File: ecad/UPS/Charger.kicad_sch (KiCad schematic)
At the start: 23 parts, among them Q1 NMOS, Q2 NMOS, Q3 NMOS, Q4 NMOS, U1 BQ25731RSNR

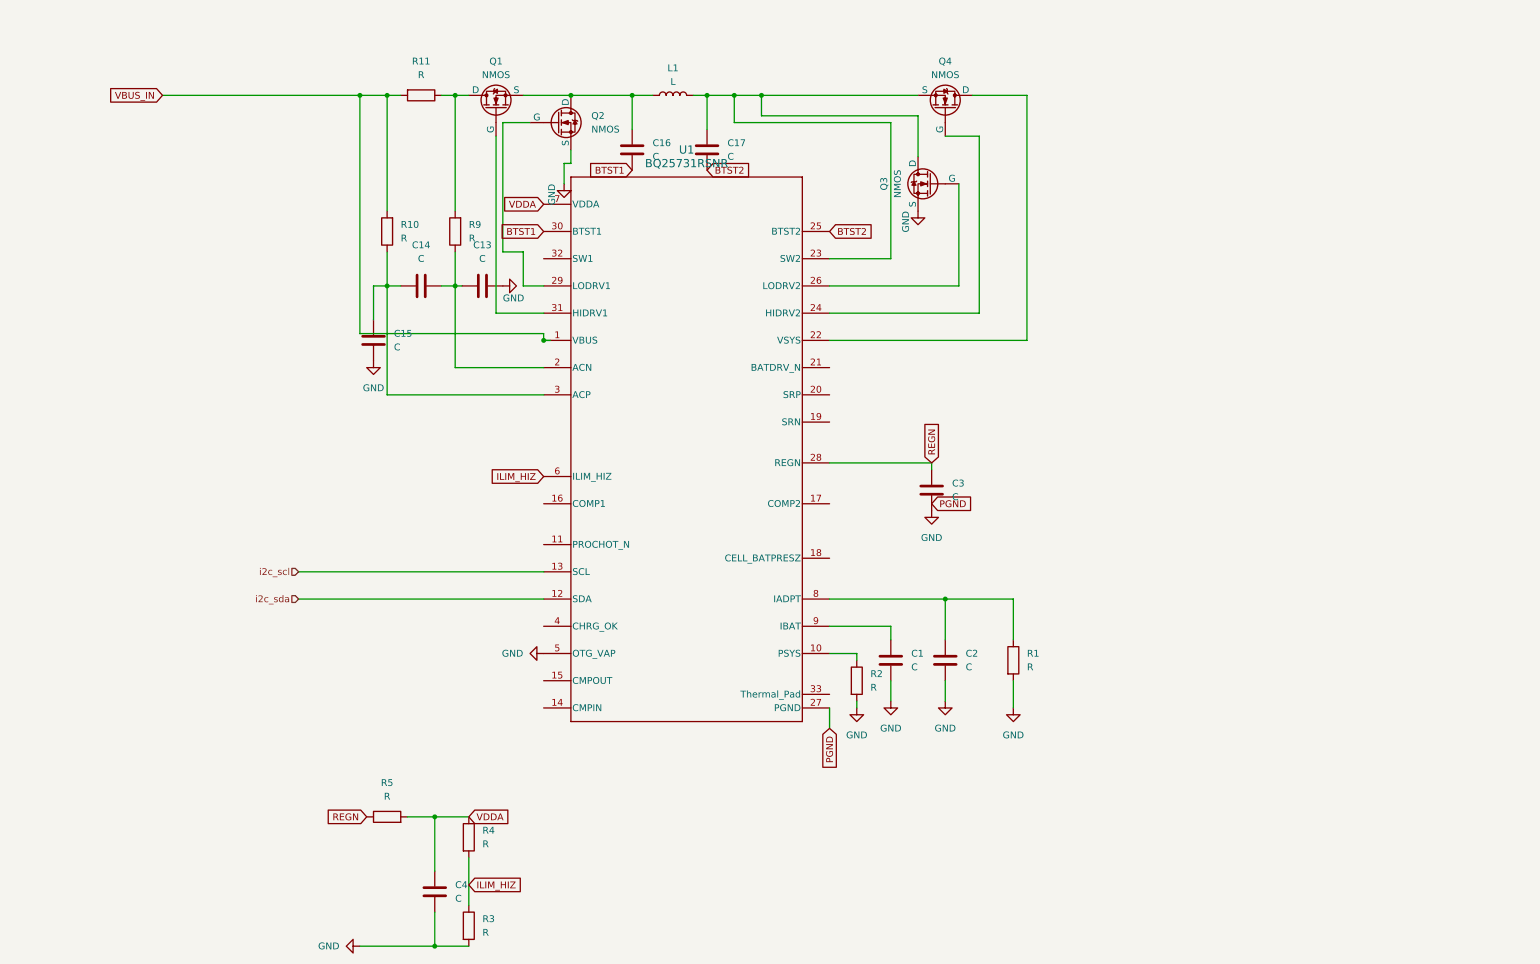
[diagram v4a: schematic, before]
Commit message: Complete most of the charger schematic
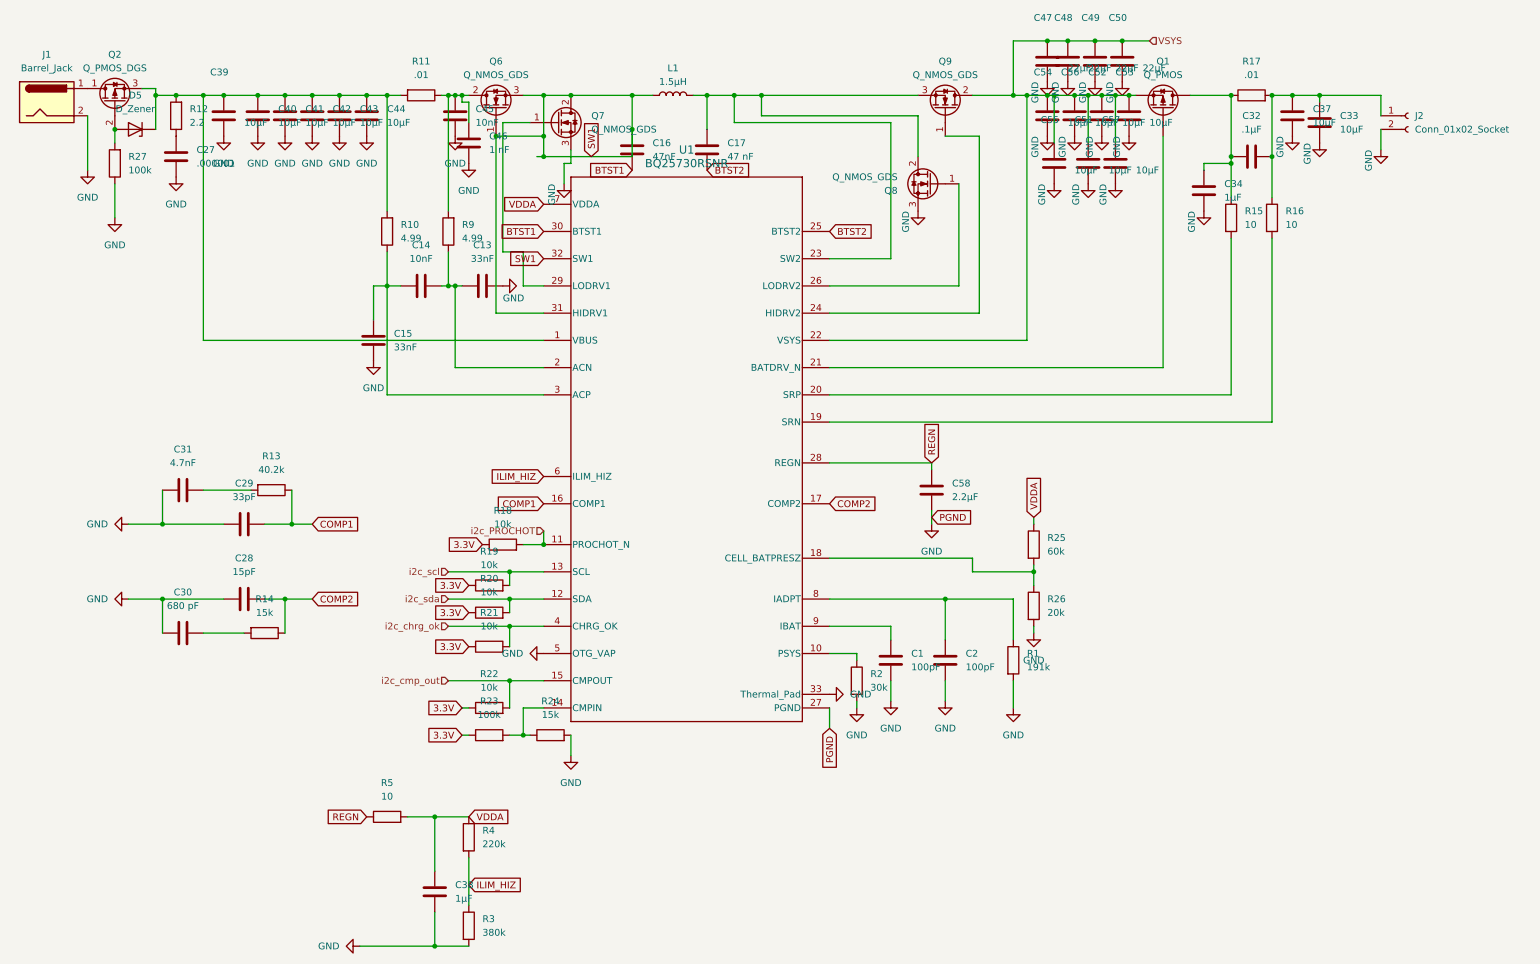
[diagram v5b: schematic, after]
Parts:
- removed C3, C4: C, symbol Device:C
- removed Q1, Q2, Q3, Q4: NMOS, symbol Simulation_SPICE:NMOS
- removed U1: BQ25731RSNR, UPS:RSN0032B-IPC_A, symbol UPS:BQ25731RSNR
- added C27: .000001, Capacitor_SMD:C_0603_1608Metric, symbol Device:C
- added C28: 15pF, Capacitor_SMD:C_0603_1608Metric, symbol Device:C
- added C29: 33pF, Capacitor_SMD:C_0603_1608Metric, symbol Device:C
- added C30: 680 pF, Capacitor_SMD:C_0603_1608Metric, symbol Device:C
- added C31: 4.7nF, Capacitor_SMD:C_0603_1608Metric, symbol Device:C
- added C32: .1µF, Capacitor_SMD:C_0603_1608Metric, symbol Device:C
- added C33, C37, C39, C40, C41, C42, C43, C44, C51, C52, C53, C54, C55, C56, C57: 10µF, Capacitor_SMD:C_0603_1608Metric, symbol Device:C
- added C34, C38: 1µF, Capacitor_SMD:C_0603_1608Metric, symbol Device:C
- added C45: 10nF, Capacitor_SMD:C_0603_1608Metric, symbol Device:C
- added C46: 1 nF, Capacitor_SMD:C_0603_1608Metric, symbol Device:C
- added C47, C48, C49, C50: 22µF, Capacitor_SMD:C_1206_3216Metric, symbol Device:C
- added C58: 2.2µF, Capacitor_SMD:C_0603_1608Metric, symbol Device:C
- added D5: D_Zener, symbol Device:D_Zener
- added J1: Barrel_Jack, symbol Connector:Barrel_Jack
- added J2: Conn_01x02_Socket, symbol Connector:Conn_01x02_Socket
- added Q1: Q_PMOS, symbol Device:Q_PMOS
- added Q2: Q_PMOS_DGS, symbol Transistor_FET:Q_PMOS_DGS
- added Q6, Q7, Q8, Q9: Q_NMOS_GDS, symbol Transistor_FET:Q_NMOS_GDS
- added R12: 2.2, Resistor_SMD:R_0805_2012Metric, symbol Device:R
- added R13: 40.2k, Resistor_SMD:R_0805_2012Metric, symbol Device:R
- added R14, R24: 15k, Resistor_SMD:R_0805_2012Metric, symbol Device:R
- added R15, R16: 10, Resistor_SMD:R_0805_2012Metric, symbol Device:R
- added R17: .01, Resistor_SMD:R_2512_6332Metric, symbol Device:R
- added R18, R19, R20, R21, R22: 10k, Resistor_SMD:R_0805_2012Metric, symbol Device:R
- added R23, R27: 100k, Resistor_SMD:R_0805_2012Metric, symbol Device:R
- added R25: 60k, Resistor_SMD:R_0805_2012Metric, symbol Device:R
- added R26: 20k, Resistor_SMD:R_0805_2012Metric, symbol Device:R
- added U1: BQ25730RSNR, UPS:RSN0032B-IPC_A, symbol UPS:BQ25730RSNR
- C1, C2: value C -> 100pF; footprint (none) -> Capacitor_SMD:C_0603_1608Metric
- C13, C15: value C -> 33nF; footprint (none) -> Capacitor_SMD:C_0603_1608Metric
- C14: value C -> 10nF; footprint (none) -> Capacitor_SMD:C_0603_1608Metric
- C16: value C -> 47nF; footprint (none) -> Capacitor_SMD:C_0603_1608Metric
- C17: value C -> 47 nF; footprint (none) -> Capacitor_SMD:C_0603_1608Metric
- L1: value L -> 1.5µH
- R1: value R -> 191k; footprint (none) -> Resistor_SMD:R_0805_2012Metric
- R10, R9: value R -> 4.99; footprint (none) -> Resistor_SMD:R_0805_2012Metric
- R11: value R -> .01; footprint (none) -> Resistor_SMD:R_2512_6332Metric
- R2: value R -> 30k; footprint (none) -> Resistor_SMD:R_0805_2012Metric
- R3: value R -> 380k; footprint (none) -> Resistor_SMD:R_0805_2012Metric
- R4: value R -> 220k; footprint (none) -> Resistor_SMD:R_0805_2012Metric
- R5: value R -> 10; footprint (none) -> Resistor_SMD:R_0805_2012Metric
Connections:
- net BTST1: now also U1.30 (BTST1)
- net BTST2: now also U1.25 (BTST2)
- net GND: now also C27.1, C28.1, C29.1, C30.1, C31.1, C33.2, C34.2, C37.2, C38.2, C39.2, C40.2, C41.2, C42.2, C43.2, C44.2, C45.2, C46.2, C47.2, C48.2, C49.2, C50.2, C51.2, C52.2, C53.2, C54.2, C55.2, C56.2, C57.2, C58.2, J1.2, J2.2 (Pin_2), Q7.3 (S), Q8.3 (S), R24.2, R26.2, R27.1, U1.27 (PGND), U1.33 (Thermal_Pad), U1.5 (OTG_VAP)
- net ILIM_HIZ: now also U1.6 (ILIM_HIZ)
- net REGN: now also C58.1, U1.28 (REGN)
- net VDDA: now also C38.1, R25.1, U1.7 (VDDA)
- net i2c_scl: now also R19.2, U1.13 (SCL)
- net i2c_sda: now also R20.2, U1.12 (SDA)
- net at C14.1, C15.2, R10.1: now also U1.3 (ACP)
- net at C13.1, C14.2, R9.1: now also U1.2 (ACN)
- net SW1: now reaches C16.2, L1.1
- net SW1: now also Q6.1 (G), Q6.3 (S), Q7.2 (D), U1.31 (HIDRV1), U1.32 (SW1)
- net at R2.1: now also U1.10 (PSYS)
- net at C1.1: now also U1.9 (IBAT)
- net at R11.1, R9.2: now also C45.1, C46.1, Q6.2 (D)
- net at C17.2, L1.2: now also Q8.2 (D), Q9.3 (S), U1.23 (SW2)
- net at C2.1, R1.1: now also U1.8 (IADPT)
- net VBUS_IN: no longer names the net of R10.2, R11.2
- net VBUS_IN: now also C39.1, C40.1, C41.1, C42.1, C43.1, C44.1, D5.1 (K), Q2.3 (S), R12.2, U1.1 (VBUS)
- new net: R23.2, R24.1, U1.14 (CMPIN)
- new net: C32.1, C33.1, C37.1, J2.1 (Pin_1), R16.1, R17.2
- new net: R16.2, U1.19 (SRN)
- new net: J1.1, Q2.1 (D)
- new net: D5.2 (A), Q2.2 (G), R27.2
- new net: C32.2, C34.1, Q1.D, R15.1, R17.1
- new net: Q9.1 (G), U1.24 (HIDRV2)
- new net: C27.2, R12.1
- new net: R25.2, R26.1, U1.18 (CELL_BATPRESZ)
- new net: Q7.1 (G), U1.29 (LODRV1)
- new net: C30.2, R14.2
- new net: R15.2, U1.20 (SRP)
- new net: C31.2, R13.2
- new net: Q1.G, U1.21 (BATDRV_N)
- new net: Q8.1 (G), U1.26 (LODRV2)
- new net 3.3V: R18.1, R19.1, R20.1, R21.1, R22.1, R23.1
- new net COMP1: C29.2, R13.1, U1.16 (COMP1)
- new net COMP2: C28.2, R14.1, U1.17 (COMP2)
- new net VSYS: C47.1, C48.1, C49.1, C50.1, C51.1, C52.1, C53.1, C54.1, C55.1, C56.1, C57.1, Q1.S, Q9.2 (D), U1.22 (VSYS)
- new net i2c_PROCHOT: R18.2, U1.11 (PROCHOT_N)
- new net i2c_chrg_ok: R21.2, U1.4 (CHRG_OK)
- new net i2c_cmp_out: R22.2, U1.15 (CMPOUT)
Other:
- title: Battery Management -> Charger
- moved on the sheet: R9

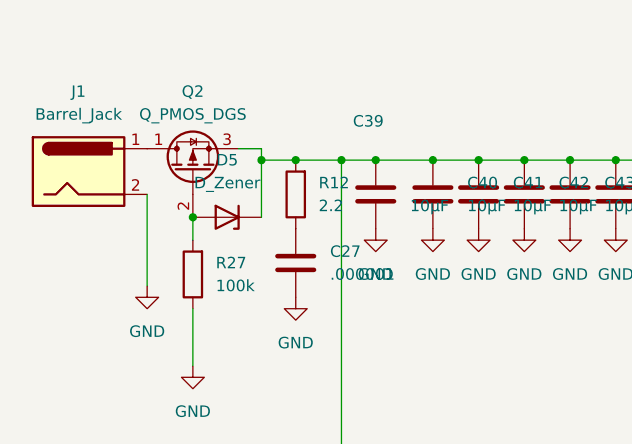
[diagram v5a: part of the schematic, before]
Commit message: Fix duplicate component names.
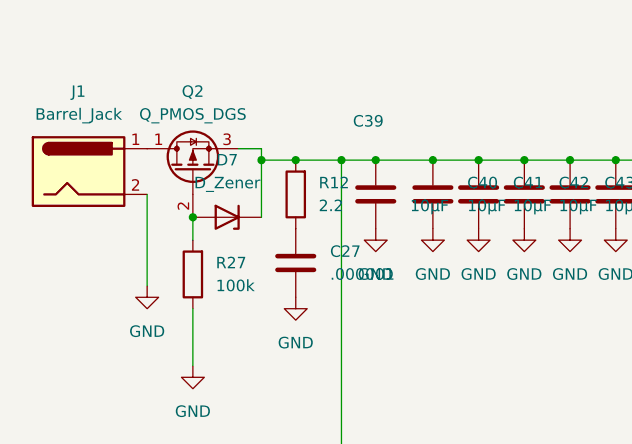
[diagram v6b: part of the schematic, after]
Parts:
- removed D5: D_Zener, symbol Device:D_Zener
- added D7: D_Zener, symbol Device:D_Zener
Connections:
- net at Q2.2 (G), R27.2: now also D7.2 (A)
- net at C39.1, C40.1, C41.1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: now also D7.1 (K)
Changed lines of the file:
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@@
 	)
 	(junction
+		(at 35.56 29.21)
+		(diameter 0)
+		(color 0 0 0 0)
+	)
+	(junction
 		(at 82.55 22.86)
 		(diameter 0)
@@
 	)
 	(junction
-		(at 35.56 29.21)
-		(diameter 0)
-		(color 0 0 0 0)
-	)
-	(junction
 		(at 67.31 22.86)
 		(diameter 0)
@@
 	)
 	(symbol
-		(lib_id "Device:D_Zener")
-		(at 39.37 29.21 180)
-		(unit 1)
-		(exclude_from_sim no)
-		(in_bom yes)
-		(on_board yes)
-		(dnp no)
-		(fields_autoplaced yes)
-		(property "Reference" "D5"
-			(at 39.37 22.86 0)
-			(effects
-				(font
-					(size 1.27 1.27)
-				)
-			)
-		)
-		(property "Value" "D_Zener"
-			(at 39.37 25.4 0)
-			(effects
-				(font
-					(size 1.27 1.27)
-				)
-			)
-		)
-		(property "Footprint" ""
-			(at 39.37 29.21 0)
-			(effects
-				(font
-					(size 1.27 1.27)
-				)
-				(hide yes)
-			)
-		)
-		(property "Datasheet" "~"
-			(at 39.37 29.21 0)
-			(effects
-				(font
-					(size 1.27 1.27)
-				)
-				(hide yes)
-			)
-		)
-		(property "Description" "Zener diode"
-			(at 39.37 29.21 0)
-			(effects
-				(font
-					(size 1.27 1.27)
-				)
-				(hide yes)
-			)
-		)
-		(pin "1"
-		)
-		(pin "2"
-		)
-		(instances
-			(project ""
-				(path "/9d92b60a-4a6b-449c-b462-cab19e69d38c/58e8621a-e50a-4c31-8927-fd6b72ccb3ce"
-					(reference "D5")
-					(unit 1)
-				)
-			)
-		)
-	)
-	(symbol
 		(lib_id "power:GND")
 		(at 55.88 30.48 0)
@@
 					(unit 1)
 				)
+			)
+		)
+	)
+	(symbol
+		(lib_id "Device:D_Zener")
+		(at 39.37 29.21 180)
+		(unit 1)
+		(exclude_from_sim no)
+		(in_bom yes)
+		(on_board yes)
+		(dnp no)
+		(fields_autoplaced yes)
+		(property "Reference" "D7"
+			(at 39.37 22.86 0)
+			(effects
+				(font
+					(size 1.27 1.27)
+				)
+			)
+		)
+		(property "Value" "D_Zener"
+			(at 39.37 25.4 0)
+			(effects
+				(font
+					(size 1.27 1.27)
+				)
+			)
+		)
+		(property "Footprint" ""
+			(at 39.37 29.21 0)
+			(effects
+				(font
+					(size 1.27 1.27)
+				)
+				(hide yes)
+			)
+		)
+		(property "Datasheet" "~"
+			(at 39.37 29.21 0)
+			(effects
+				(font
+					(size 1.27 1.27)
+				)
+				(hide yes)
+			)
+		)
+		(property "Description" "Zener diode"
+			(at 39.37 29.21 0)
+			(effects
+				(font
+					(size 1.27 1.27)
+				)
+				(hide yes)
+			)
+		)
+		(pin "1"
+		)
+		(pin "2"
+		)
+		(instances
+			(project "UPS"
+				(path "/9d92b60a-4a6b-449c-b462-cab19e69d38c/58e8621a-e50a-4c31-8927-fd6b72ccb3ce"
+					(reference "D7")
+					(unit 1)
+				)

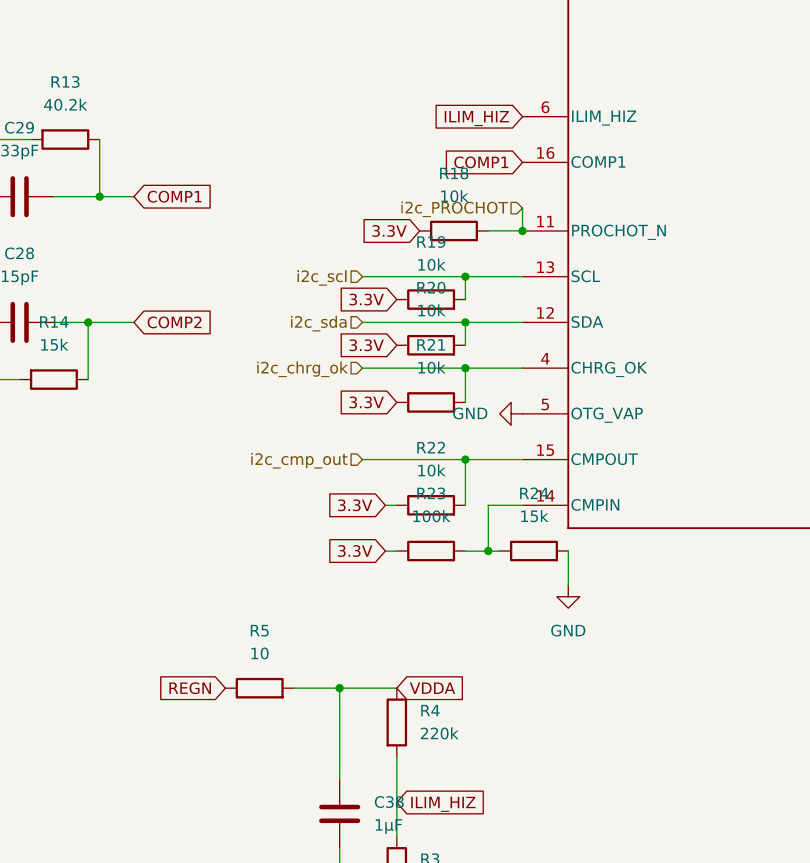
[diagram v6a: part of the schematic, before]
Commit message: mcu fixed
fixed i2c and gpio and boot and decoupler and add 3.3 regulator.
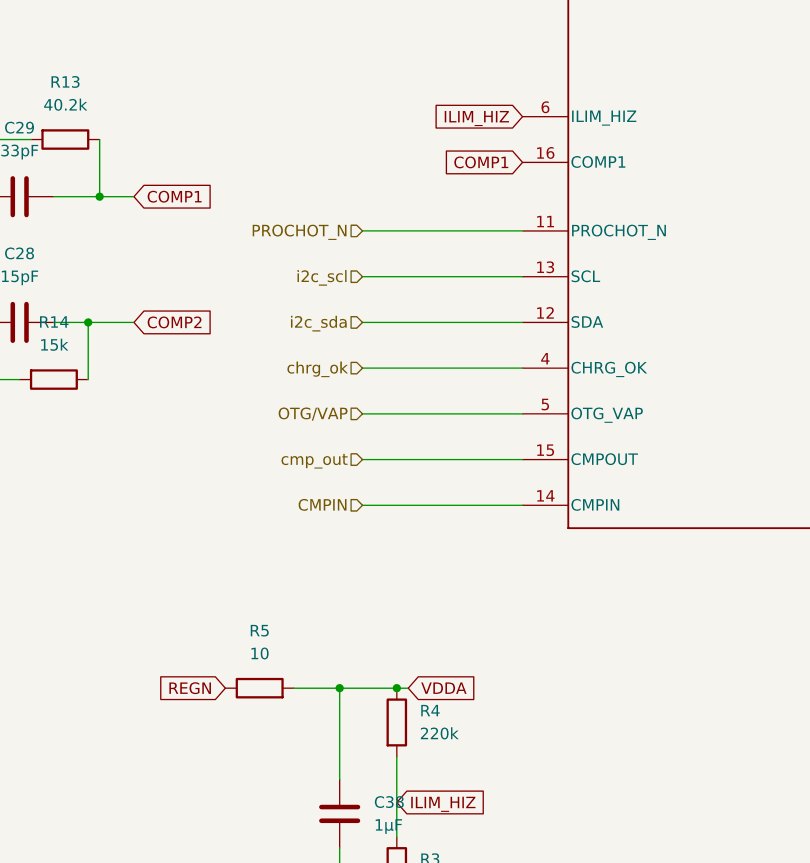
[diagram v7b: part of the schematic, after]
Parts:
- removed R18, R19, R20, R21, R22: 10k, Resistor_SMD:R_0805_2012Metric, symbol Device:R
- removed R23: 100k, Resistor_SMD:R_0805_2012Metric, symbol Device:R
- removed R24: 15k, Resistor_SMD:R_0805_2012Metric, symbol Device:R
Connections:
- net GND: no longer U1.5 (OTG_VAP)
- net CMPIN: now reaches U1.14 (CMPIN)
- net i2c_PROCHOT renamed PROCHOT_N
- net i2c_chrg_ok renamed chrg_ok
- net i2c_cmp_out renamed cmp_out
- new net OTG/VAP: U1.5 (OTG_VAP)
